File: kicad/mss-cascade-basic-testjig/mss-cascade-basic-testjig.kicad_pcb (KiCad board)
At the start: 2 copper layers, 101.6 x 120.7 mm, 101 parts, among them J1 PJ-202A, J11 Molex 0532610471, J12 Molex 0532610471, J2 SM04B-SRSS, J3 SM04B-SRSS, J4 SM04B-SRSS, J5 8P8C, J6 8P8C, Q1 ZXMS6004FF, Q10 ZXMS6004FF, Q11 ZXMS6004FF, Q12 ZXMS6004FF, Q2 ZXMS6004FF, Q3 ZXMS6004FF, Q4 ZXMS6004FF, Q5 ZXMS6004FF, Q6 ZXMS6004FF, Q7 ZXMS6004FF, Q8 ZXMS6004FF, Q9 ZXMS6004FF, SW1 FSM4JSMATR, SW2 FSM4JSMATR, U1 AP7381-50, U11 PCA9555PW, U2 DRV8872DDA, U3 74HC4049, U4 INA219AxD, U5 ProMicro

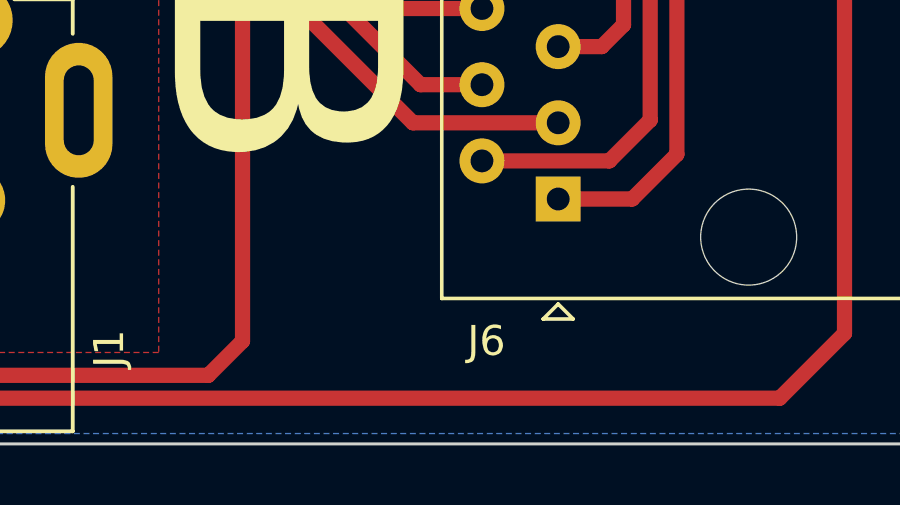
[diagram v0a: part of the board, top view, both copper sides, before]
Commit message: Fix issues with wire naming
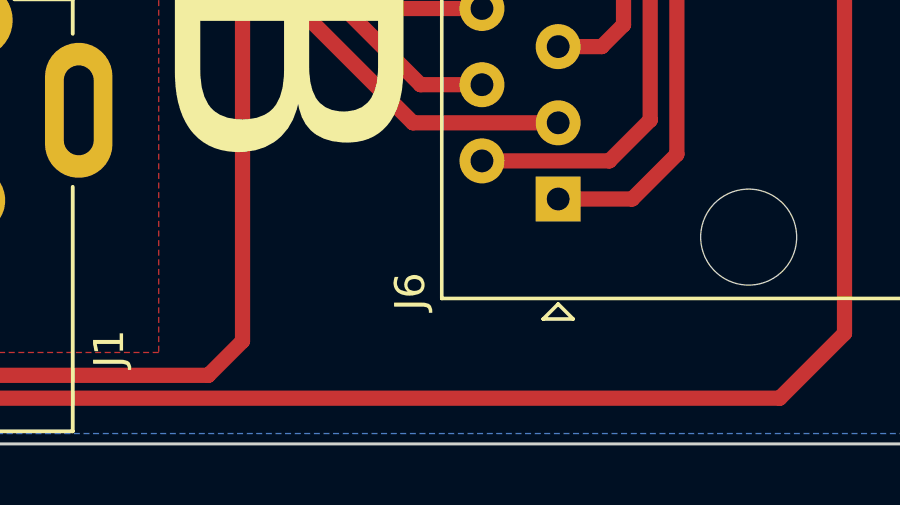
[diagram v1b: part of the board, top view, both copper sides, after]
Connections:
- U11 pad 10: /MSS_B_AA_OUT -> /MSS_B_S_OUT
- U11 pad 11: /MSS_B_A_OUT -> /MSS_B_AA_OUT
- U11 pad 13: /MSS_A_A_OUT -> /MSS_A_AA_OUT
- U11 pad 14: /MSS_A_AA_OUT -> /MSS_A_S_OUT
- U11 pad 15: /MSS_A_S_OUT -> /MSS_A_A_OUT
- U11 pad 16: /MSS_B_S_OUT -> /MSS_B_A_OUT
- U3 pad 10: /MSS_A_S_OUT -> /MSS_A_A_OUT
- U3 pad 12: /MSS_A_AA_OUT -> /MSS_A_S_OUT
- U3 pad 15: /MSS_A_A_OUT -> /MSS_A_AA_OUT
- U3 pad 2: /MSS_B_A_OUT -> /MSS_B_AA_OUT
- U3 pad 4: /MSS_B_AA_OUT -> /MSS_B_S_OUT
- U3 pad 6: /MSS_B_S_OUT -> /MSS_B_A_OUT
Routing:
- net /MSS_A_A_OUT: track 10.9 -> 19.7 mm
- net /MSS_B_A_OUT: track 12.0 -> 19.8 mm
- net /MSS_A_AA_OUT: track 15.9 -> 10.9 mm
- net /MSS_B_S_OUT: track 19.8 -> 15.9 mm
- net /MSS_B_AA_OUT: track 15.9 -> 12.0 mm
- net /MSS_A_S_OUT: track 19.7 -> 15.9 mm
